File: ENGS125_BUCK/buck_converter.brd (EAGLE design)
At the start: 100 x 80 mm, 19 parts, among them M1 IPD220N06L3, M2 IPD220N06L3, U1 LTC6992, U2 LTC4449

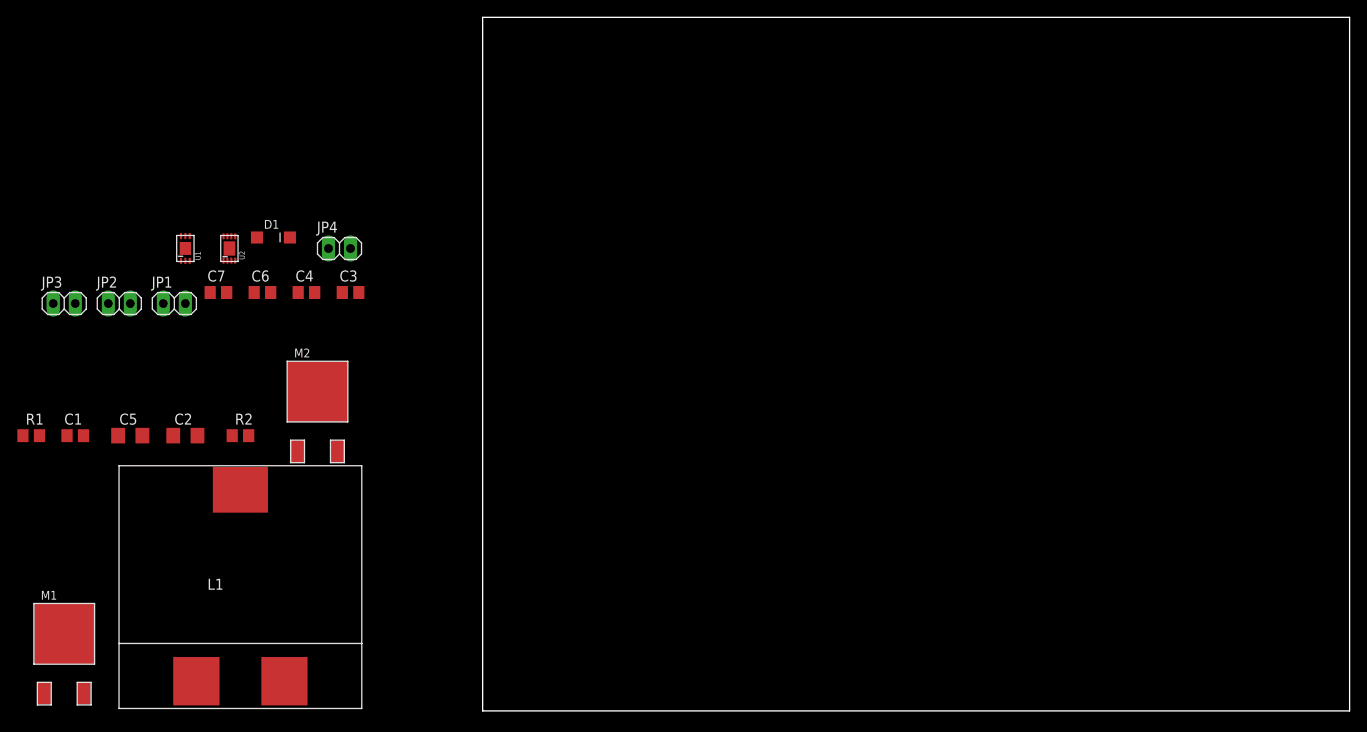
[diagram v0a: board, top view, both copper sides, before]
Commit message: Completed initial component placement
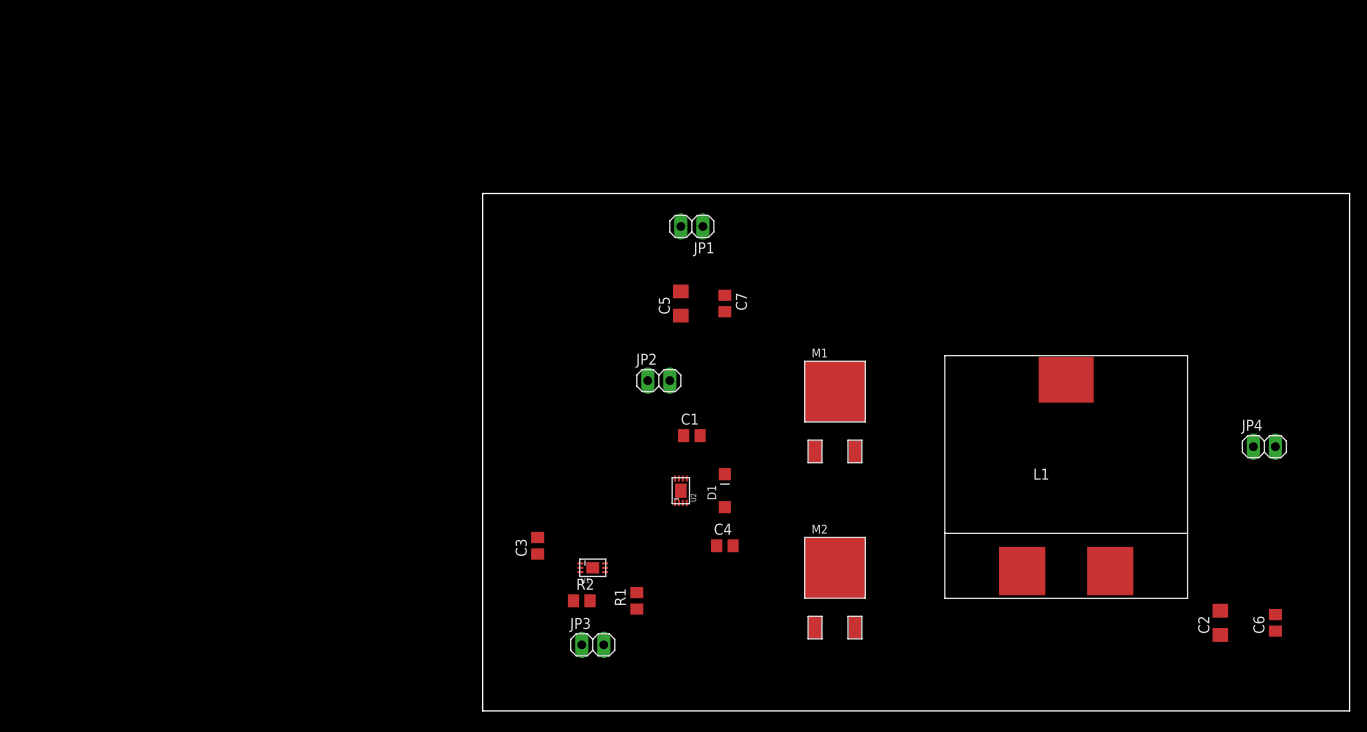
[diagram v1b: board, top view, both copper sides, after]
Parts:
- moved C6 122.9 mm to (91.4, 10.2), turned to 90 degrees
- moved C2 121.3 mm to (85.1, 10.2), turned to 90 degrees
- moved JP4 109.1 mm to (90.2, 30.5)
- moved L1 96.1 mm to (67.3, 30.5)
- moved M1 93.2 mm to (40.6, 36.8)
- moved JP3 72.6 mm to (12.7, 7.62)
- moved R1 72.4 mm to (17.8, 12.7), turned to 90 degrees
- moved C1 71.1 mm to (24.1, 31.8)
- moved C5 65.3 mm to (22.9, 47.0), turned to 90 degrees
- moved M2 63.1 mm to (40.6, 16.5)
- moved JP2 62.9 mm to (20.3, 38.1)
- moved JP1 60.3 mm to (24.1, 55.9), turned to 180 degrees
- moved D1 59.7 mm to (27.9, 25.4), turned to 90 degrees
- moved U1 59.7 mm to (12.7, 16.5), turned to 270 degrees
- moved U2 59.1 mm to (22.9, 25.4)
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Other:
- board size 100 x 80 mm -> 100 x 59.7 mm

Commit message: Defined board shape and added mounting holes to corners
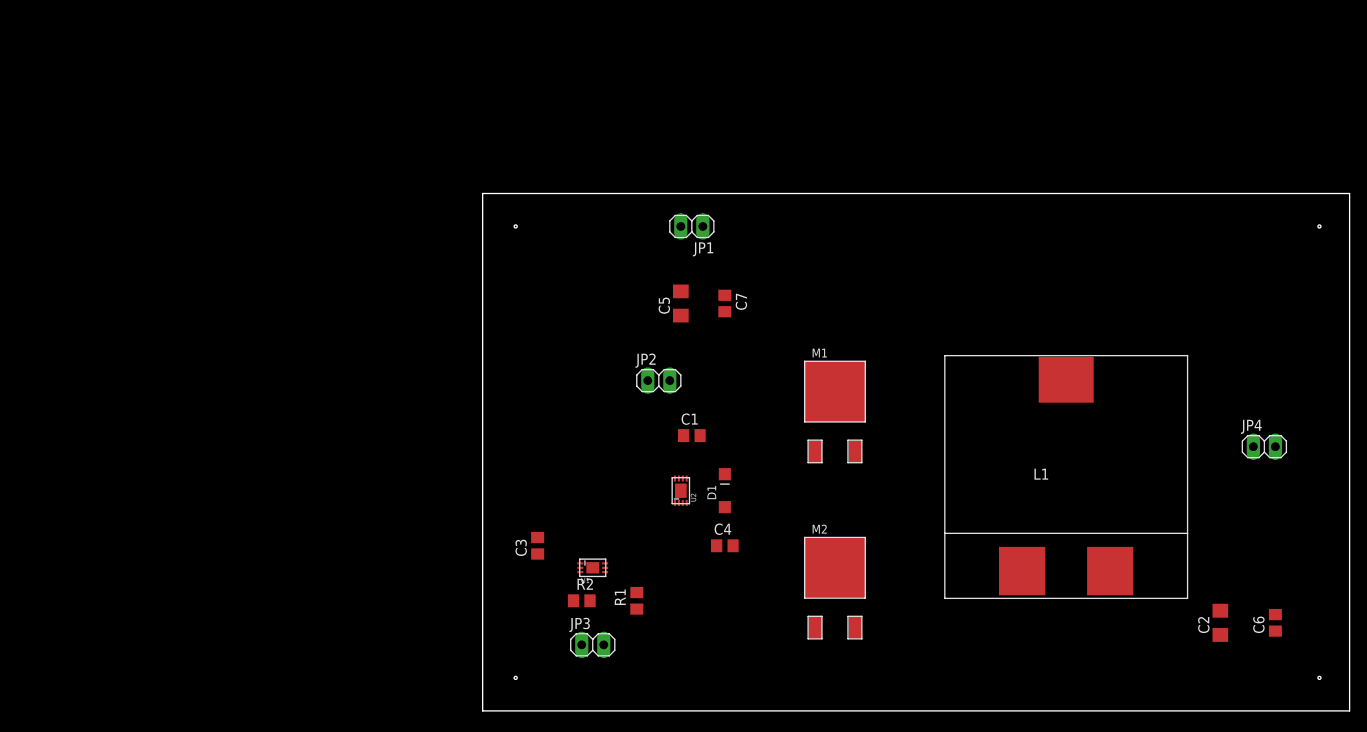
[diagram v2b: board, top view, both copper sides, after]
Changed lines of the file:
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@@
 <layer number="43" name="vRestrict" color="2" fill="10" visible="yes" active="yes"/>
 <layer number="44" name="Drills" color="7" fill="1" visible="no" active="yes"/>
-<layer number="45" name="Holes" color="7" fill="1" visible="no" active="yes"/>
+<layer number="45" name="Holes" color="7" fill="1" visible="yes" active="yes"/>
 <layer number="46" name="Milling" color="3" fill="1" visible="no" active="yes"/>
 <layer number="47" name="Measures" color="7" fill="1" visible="no" active="yes"/>
@@
 <wire x1="100" y1="59.68" x2="0" y2="59.68" width="0" layer="20"/>
 <wire x1="0" y1="59.68" x2="0" y2="0" width="0" layer="20"/>
+<hole x="3.81" y="55.88" drill="0.35" locked="yes"/>
+<hole x="96.52" y="55.88" drill="0.35" locked="yes"/>
+<hole x="96.52" y="3.81" drill="0.35" locked="yes"/>
+<hole x="3.81" y="3.81" drill="0.35" locked="yes"/>
 </plain>
 <attributes>
@@
 <contactref element="R1" pad="1"/>
 <contactref element="JP3" pad="2"/>
-<wire x1="14.125" y1="16.01" x2="17.78" y2="11.75" width="0" layer="19" extent="1-1"/>
+<wire x1="17.78" y1="11.75" x2="14.125" y2="16.01" width="0" layer="19" extent="1-1"/>
 <wire x1="13.97" y1="7.62" x2="17.78" y2="11.75" width="0" layer="19" extent="1-1"/>
 </signal>
@@
 <contactref element="C1" pad="2"/>
 <contactref element="U2" pad="2"/>
-<wire x1="62.23" y1="16.129" x2="42.94" y2="29.93" width="0" layer="19" extent="1-1"/>
+<wire x1="40.64" y1="16.51" x2="62.23" y2="16.129" width="0" layer="19" extent="1-1"/>
+<wire x1="42.94" y1="29.93" x2="40.64" y2="16.51" width="0" layer="19" extent="1-1"/>
 <wire x1="25.08" y1="31.75" x2="42.94" y2="29.93" width="0" layer="19" extent="1-1"/>
 <wire x1="22.635" y1="24" x2="25.08" y2="31.75" width="0" layer="19" extent="1-1"/>
-<wire x1="40.64" y1="16.51" x2="22.635" y2="24" width="0" layer="19" extent="1-1"/>
 </signal>
 <signal name="VOUT">
@@
 <contactref element="C2" pad="1"/>
 <contactref element="C6" pad="1"/>
-<wire x1="85.09" y1="8.76" x2="72.39" y2="16.129" width="0" layer="19" extent="1-1"/>
-<wire x1="91.44" y1="9.21" x2="85.09" y2="8.76" width="0" layer="19" extent="1-1"/>
-<wire x1="88.9" y1="30.48" x2="72.39" y2="16.129" width="0" layer="19" extent="1-1"/>
+<wire x1="91.44" y1="9.21" x2="88.9" y2="30.48" width="0" layer="19" extent="1-1"/>
+<wire x1="85.09" y1="8.76" x2="91.44" y2="9.21" width="0" layer="19" extent="1-1"/>
+<wire x1="72.39" y1="16.129" x2="85.09" y2="8.76" width="0" layer="19" extent="1-1"/>
 </signal>
 <signal name="VIN">
@@
 <contactref element="M1" pad="D"/>
 <contactref element="C5" pad="1"/>
-<wire x1="27.94" y1="47.94" x2="40.64" y2="36.83" width="0" layer="19" extent="1-1"/>
-<wire x1="25.4" y1="55.88" x2="27.94" y2="47.94" width="0" layer="19" extent="1-1"/>
+<wire x1="27.94" y1="47.94" x2="25.4" y2="55.88" width="0" layer="19" extent="1-1"/>
 <wire x1="22.86" y1="45.59" x2="27.94" y2="47.94" width="0" layer="19" extent="1-1"/>
+<wire x1="40.64" y1="36.83" x2="27.94" y2="47.94" width="0" layer="19" extent="1-1"/>
 </signal>
 <signal name="BG">
@@
 packages will not be understood (or retained) with this version.
 </note>
+<note version="8.5" severity="warning">
+Since Version 8.5, EAGLE supports locking for holes, vias, wires and polygons.
+The locking property on all objects of these types will not be understood in this version.
+</note>
 </compatibility>

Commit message: Added power polygons to top layer
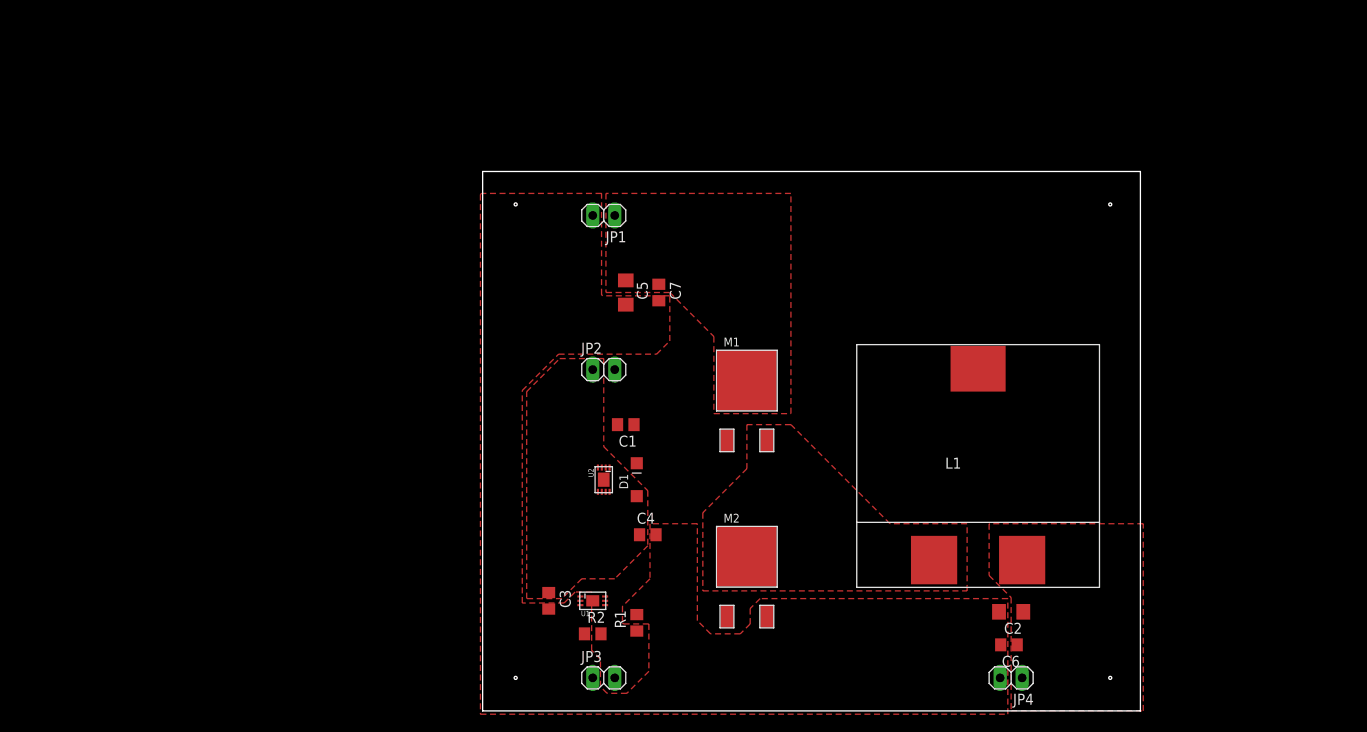
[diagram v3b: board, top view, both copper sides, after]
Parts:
- moved JP4 39.6 mm to (61.0, 3.81), turned to 180 degrees
- moved C6 30.8 mm to (60.7, 7.62), turned to 180 degrees
- moved C2 24.2 mm to (61.0, 11.4), turned to 180 degrees
- moved L1 10.2 mm to (57.1, 31.8)
- moved D1 10.2 mm to (17.8, 26.7)
- moved M1 10.2 mm to (30.5, 38.1)
- moved M2 10.2 mm to (30.5, 17.8)
- moved JP1 10.2 mm to (14.0, 57.1)
- moved C4 8.98 mm to (19.1, 20.3)
- moved U2 8.98 mm to (14.0, 26.7), turned to 180 degrees
- moved C7 7.73 mm to (20.3, 48.3)
- moved C1 7.73 mm to (16.5, 33.0), turned to 180 degrees
- moved C3 6.48 mm to (7.62, 12.7), turned to 270 degrees
- moved JP2 6.48 mm to (14.0, 39.4)
- moved C5 6.48 mm to (16.5, 48.3), turned to 270 degrees
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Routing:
- added copper zone on layer 1, net GND
- added copper zone on layer 1, net VGG
- added copper zone on layer 1, net VIN
- added copper zone on layer 1, net VOUT
- added copper zone on layer 1, net VSW
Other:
- board size 100 x 59.7 mm -> 75.9 x 62.2 mm

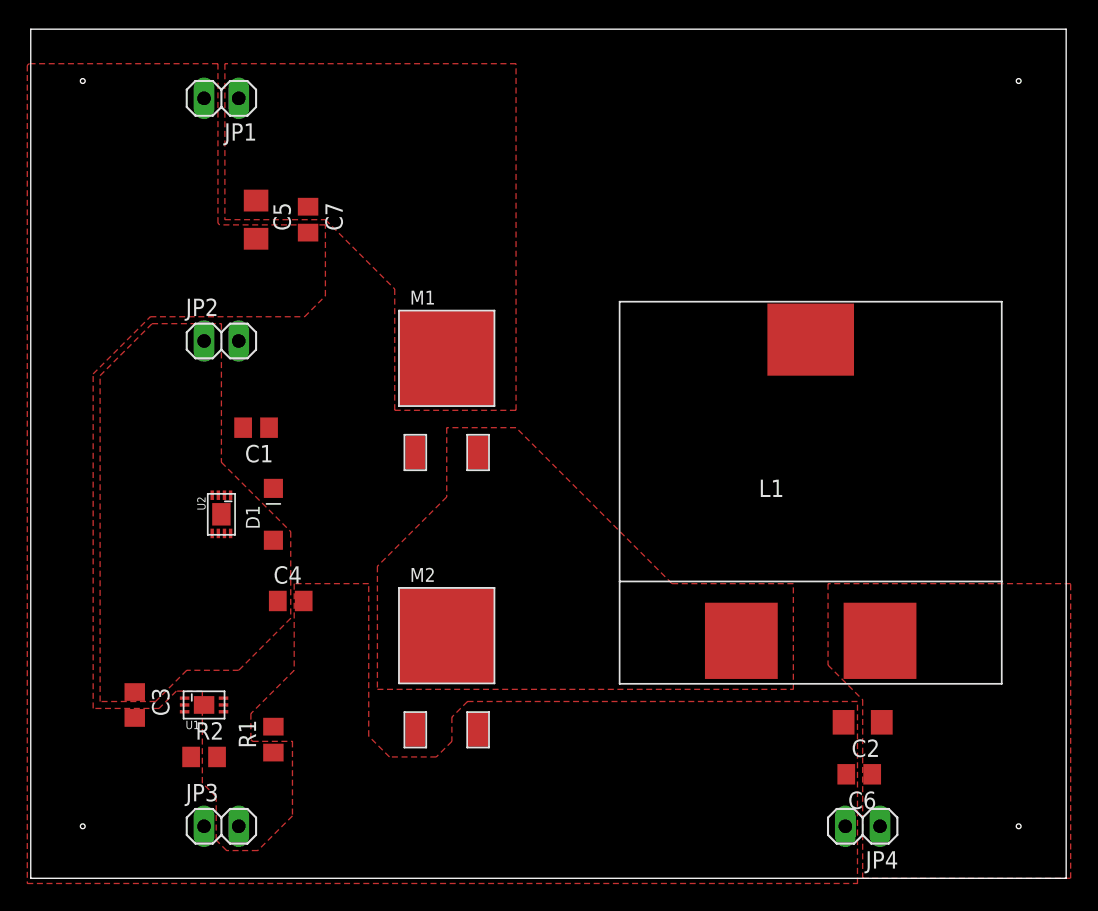
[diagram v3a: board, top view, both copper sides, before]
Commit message: Added GND plane on bottom layer and completed routing
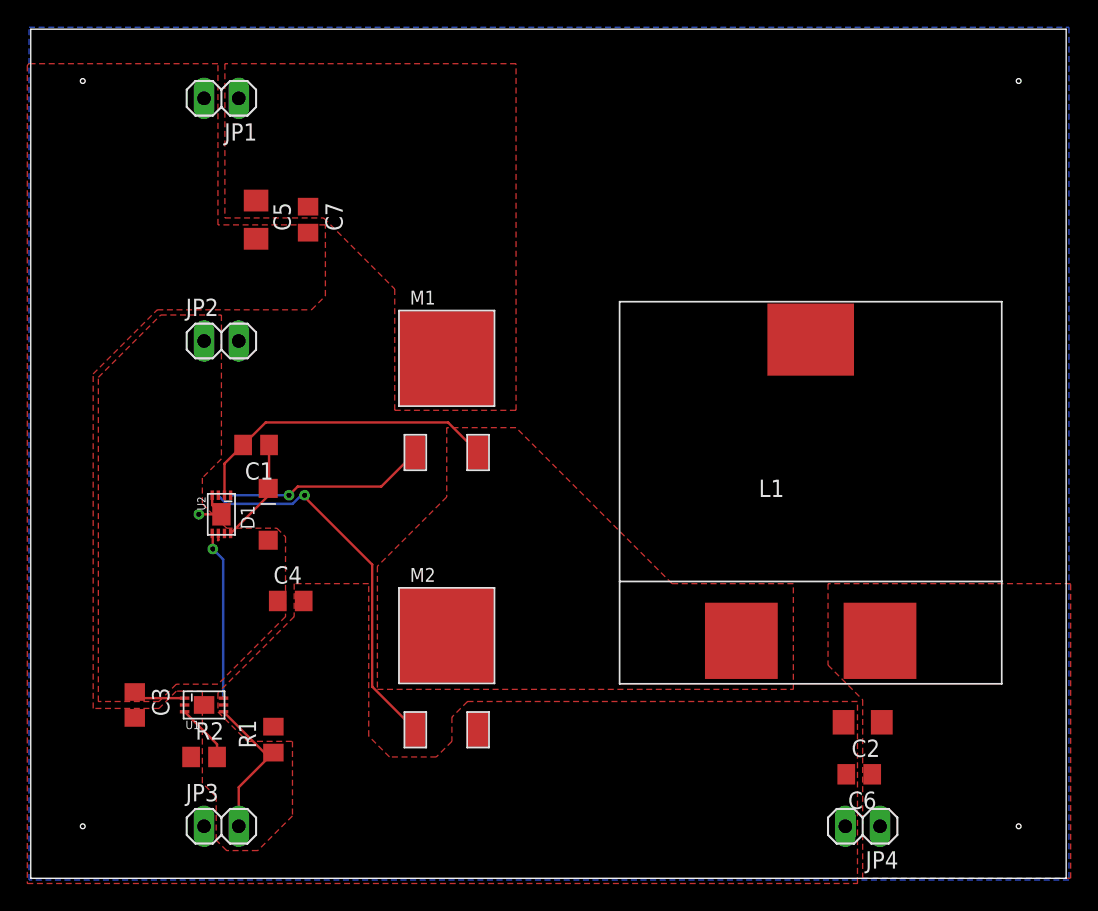
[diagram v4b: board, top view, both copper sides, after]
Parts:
- moved C1 1.27 mm to (16.5, 31.8)
- moved D1 0.38 mm to (17.4, 26.7)
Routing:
- net BG: track 0.00 -> 27.4 mm, vias 0 -> 1
- net VSW: track 0.00 -> 23.1 mm
- net TG: track 0.00 -> 14.7 mm, vias 0 -> 1
- net VPWM: track 0.00 -> 12.4 mm, vias 0 -> 1
- net VMOD: track 0.00 -> 11.3 mm
- net N$2: track 0.00 -> 7.77 mm
- net VGG: track 0.00 -> 4.36 mm
- net N$1: track 0.00 -> 4.29 mm
- net GND: track 0.00 -> 3.33 mm, vias 0 -> 1
- added copper zone on layer 16, net GND
